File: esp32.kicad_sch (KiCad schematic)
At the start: 13 parts, among them J1 DIN-5_180degree, J2 DIN-5_180degree, U1 ESP32-S3-DevKitC, U3 6N138, U4 6N138

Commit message: New official footprints for DIN/RCA
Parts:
- J1, J2: footprint (none) -> noaidi-fpga-synth:Lumberg_0105_05
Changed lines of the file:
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@@
 			)
 		)
-		(property "Footprint" ""
+		(property "Footprint" "noaidi-fpga-synth:Lumberg_0105_05"
 			(at 196.85 83.82 0)
 			(hide yes)
@@
 			)
 		)
-		(property "Footprint" ""
+		(property "Footprint" "noaidi-fpga-synth:Lumberg_0105_05"
 			(at 196.85 121.92 0)
 			(hide yes)

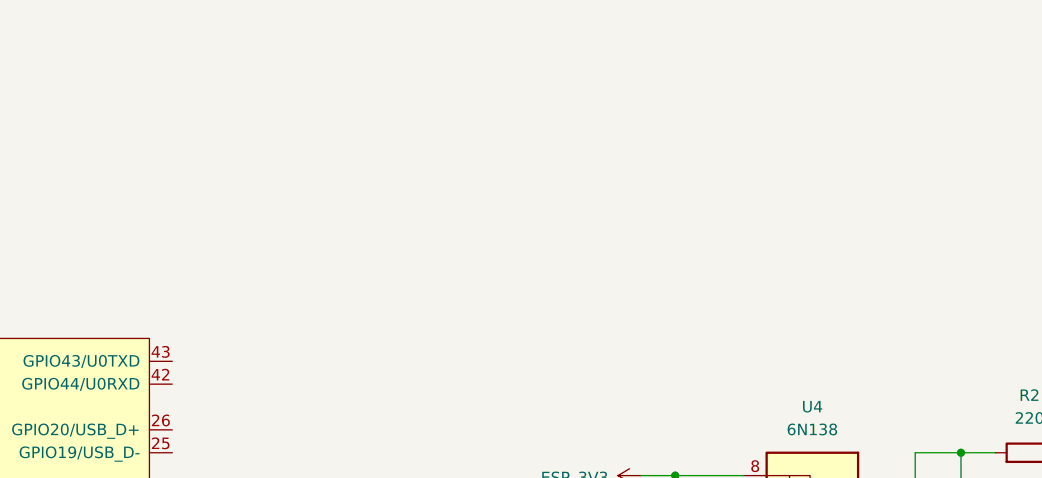
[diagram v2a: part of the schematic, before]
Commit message: Added LM66100 ideal diodes for power source switching.
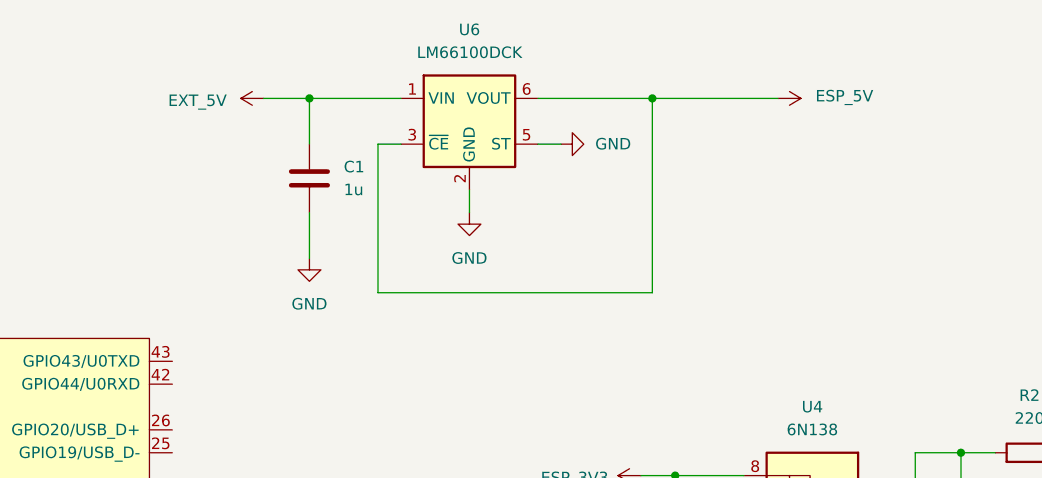
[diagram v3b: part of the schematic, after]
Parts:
- added C1: 1u, symbol Device:C
- added U6: LM66100DCK, Package_TO_SOT_SMD:SOT-363_SC-70-6, symbol Power_Management:LM66100DCK
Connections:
- net ESP_5V: now also U6.3 (~{CE}), U6.6 (VOUT)
- net GND: now also C1.2, U6.2 (GND), U6.5 (ST)
- new net EXT_5V: C1.1, U6.1 (VIN)
